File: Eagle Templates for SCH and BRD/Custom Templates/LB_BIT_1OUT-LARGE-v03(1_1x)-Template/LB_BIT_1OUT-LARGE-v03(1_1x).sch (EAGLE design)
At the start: 7 parts, among them P1BSF1 BITSNAP_V03_FEMALE, U6 LV321SOT23-5

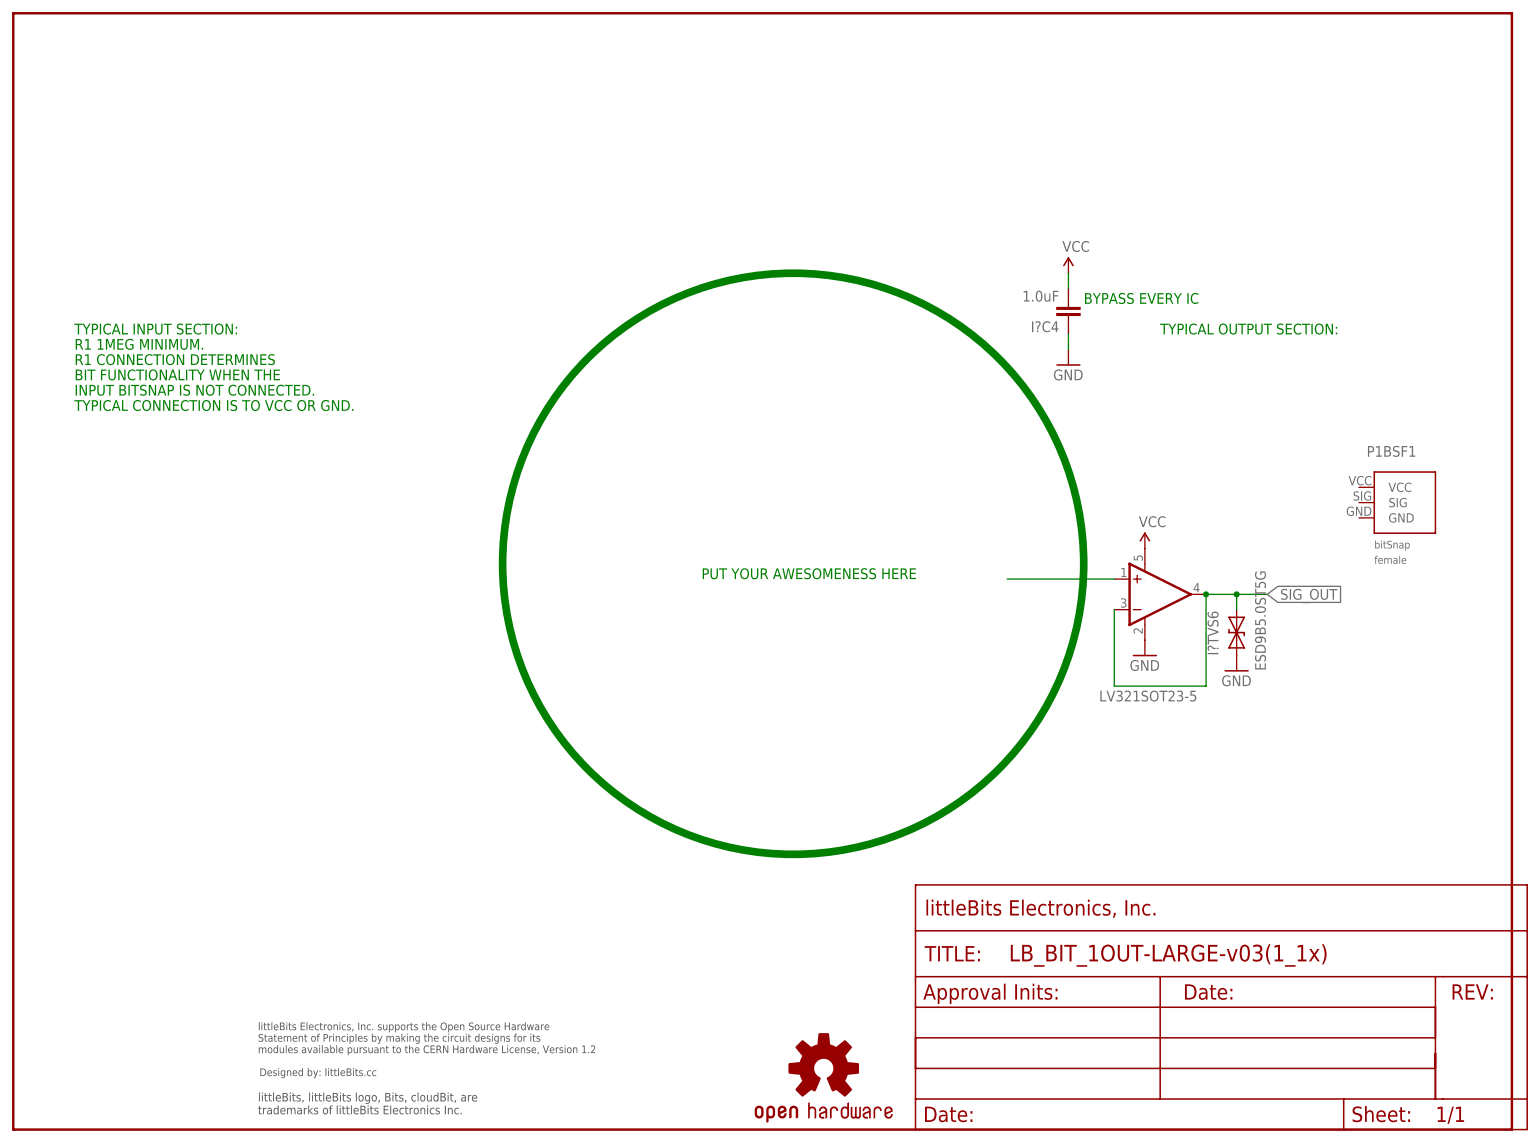
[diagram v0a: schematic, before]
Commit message: Updated templates
- Added ferrite beads
- Moved text and annotations off of Nets layer
- Minor layout changes
- Removed I/O/W prefix from reference designators
- Removed output stage components from output bits
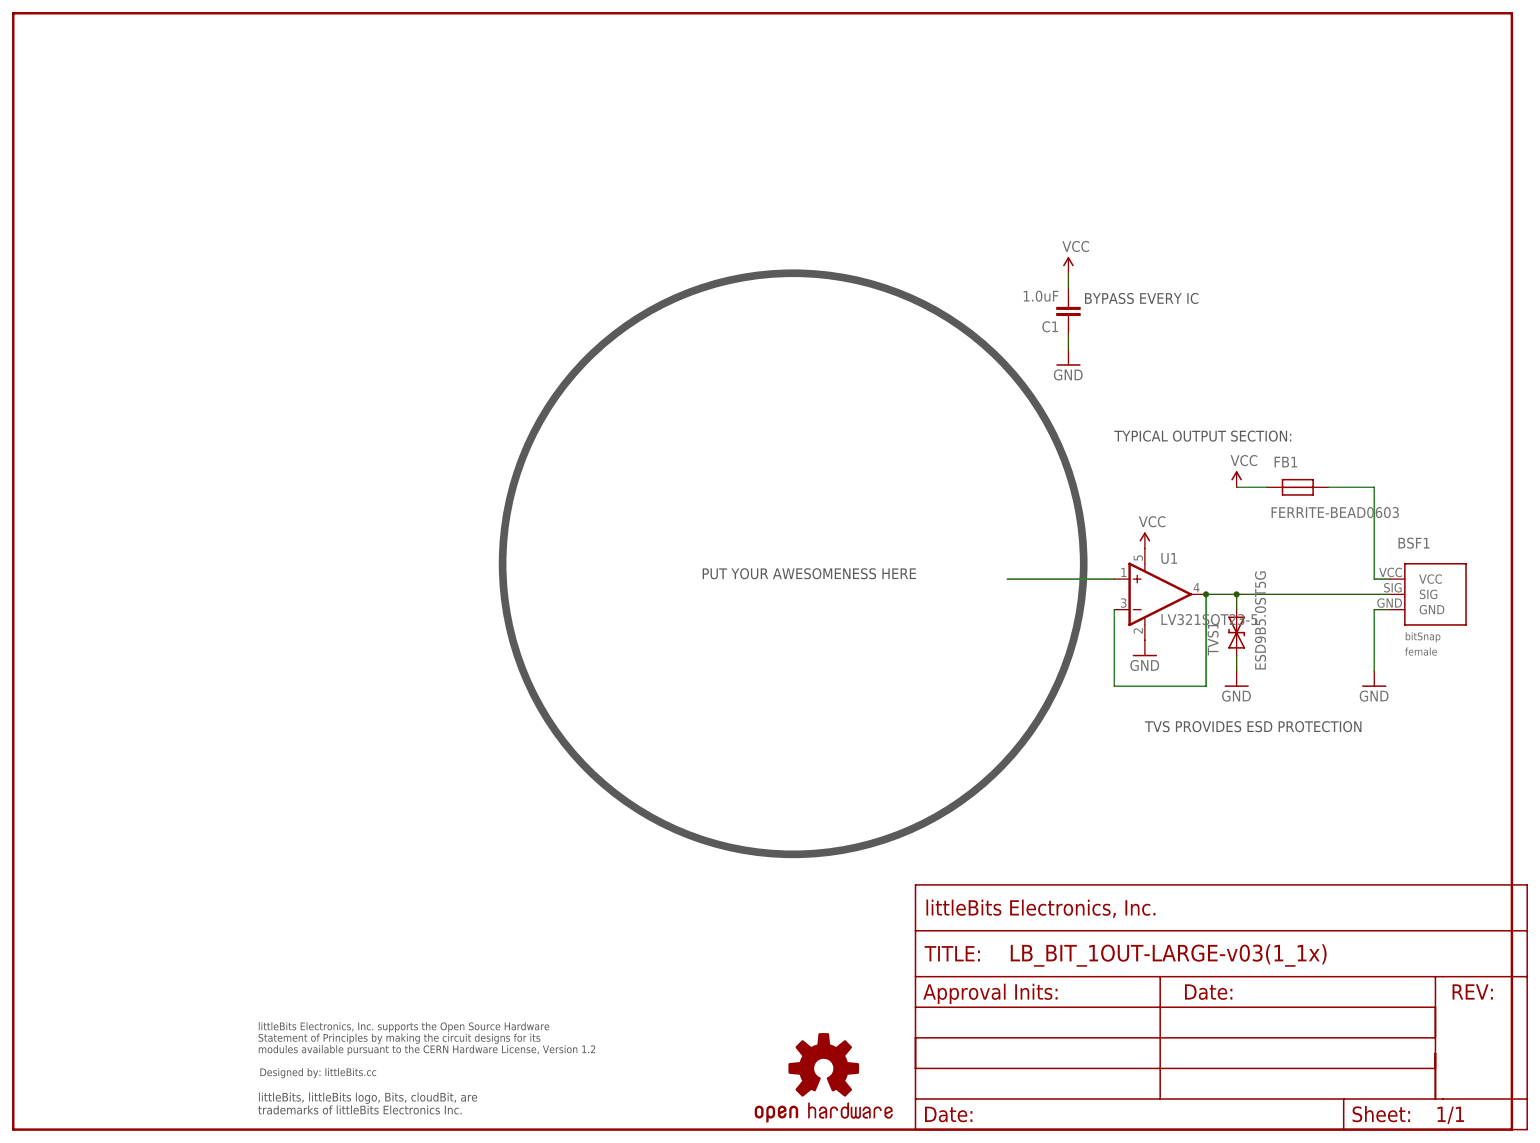
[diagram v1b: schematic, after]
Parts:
- removed P1BSF1: BITSNAP_V03_FEMALE, bitSnap:BITSNAP_V03_FEMALE
- added BSF1: BITSNAP_V03_FEMALE, bitSnap:BITSNAP_V03_FEMALE
- added FB1: FERRITE-BEAD0603, LITTLEBITS:FERRITE-BEAD0603
- FRAME1: value FRAME-LETTER -> FRAME-LETTERWHITEMASK; device LITTLEBITS:FRAME-LETTER -> LITTLEBITS:FRAME-LETTERWHITEMASK
- renumbered I?C4 to C1, I?TVS6 to TVS1, U6 to U1
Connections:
- new net N$2: BSF1.VCC, FB1.P$1
- net GND: now also BSF1.GND
- net SIG_OUT: now also BSF1.SIG
- net VCC: now also FB1.P$2
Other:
- note added: "TVS PROVIDES ESD PROTECTION"
- note removed: "BIT FUNCTIONALITY WHEN THE"
- note removed: "INPUT BITSNAP IS NOT CONNECTED."
- note removed: "R1 1MEG MINIMUM."
- note removed: "R1 CONNECTION DETERMINES"
- note removed: "TYPICAL CONNECTION IS TO VCC OR GND."
- note removed: "TYPICAL INPUT SECTION:"
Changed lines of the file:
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@@
 <?xml version="1.0" encoding="utf-8"?>
 <!DOCTYPE eagle SYSTEM "eagle.dtd">
-<eagle version="6.6.0">
+<eagle version="6.5.0">
 <drawing>
 <settings>
@@
 <layer number="56" name="wert" color="7" fill="1" visible="no" active="no"/>
 <layer number="57" name="tCAD" color="7" fill="1" visible="no" active="no"/>
+<layer number="90" name="Modules" color="5" fill="1" visible="no" active="yes"/>
 <layer number="91" name="Nets" color="2" fill="1" visible="yes" active="yes"/>
 <layer number="92" name="Busses" color="1" fill="1" visible="yes" active="yes"/>
@@
 <layer number="97" name="Info" color="7" fill="1" visible="yes" active="yes"/>
 <layer number="98" name="Guide" color="6" fill="1" visible="yes" active="yes"/>
+<layer number="99" name="SpiceOrder" color="7" fill="1" visible="no" active="no"/>
 <layer number="100" name="Muster" color="7" fill="1" visible="no" active="no"/>
 <layer number="101" name="Patch_Top" color="12" fill="4" visible="yes" active="yes"/>
@@
 <layer number="251" name="SMDround" color="12" fill="11" visible="no" active="no"/>
 <layer number="254" name="cooling" color="7" fill="1" visible="yes" active="yes"/>
+<layer number="255" name="routoute" color="7" fill="1" visible="no" active="yes"/>
 </layers>
 <schematic>
@@
 <parts>
 <part name="U$3" library="SparkFun" deviceset="OSHW-LOGO" device="L"/>
-<part name="P1BSF1" library="bitSnap" deviceset="BITSNAP_V03_FEMALE" device=""/>
-<part name="I?C4" library="LITTLEBITS" deviceset="CAP" device="CAP-0603" value="1.0uF">
+<part name="BSF1" library="bitSnap" deviceset="BITSNAP_V03_FEMALE" device=""/>
+<part name="C1" library="LITTLEBITS" deviceset="CAP" device="CAP-0603" value="1.0uF">
 <attribute name="COMPOSITION" value=""/>
 <attribute name="LB_PN" value=""/>
@@
 <part name="GND17" library="SparkFun" deviceset="GND" device=""/>
 <part name="P+2" library="SparkFun" deviceset="VCC" device=""/>
-<part name="U6" library="LITTLEBITS" deviceset="LV321" device="SOT23-5"/>
+<part name="U1" library="LITTLEBITS" deviceset="LV321" device="SOT23-5"/>
 <part name="GND18" library="SparkFun" deviceset="GND" device=""/>
 <part name="P+3" library="SparkFun" deviceset="VCC" device=""/>
 <part name="GND19" library="SparkFun" deviceset="GND" device=""/>
-<part name="I?TVS6" library="LITTLEBITS" deviceset="DIODE-TVS" device="SOD-923" value="ESD9B5.0ST5G"/>
+<part name="TVS1" library="LITTLEBITS" deviceset="DIODE-TVS" device="SOD-923" value="ESD9B5.0ST5G"/>
 <part name="U$4" library="LITTLEBITS" deviceset="OSHWCREDIT" device=""/>
-<part name="FRAME1" library="LITTLEBITS" deviceset="FRAME-LETTER" device=""/>
+<part name="FRAME1" library="LITTLEBITS" deviceset="FRAME-LETTER" device="WHITEMASK"/>
+<part name="FB1" library="LITTLEBITS" deviceset="FERRITE-BEAD" device="0603"/>
+<part name="GND1" library="SparkFun" deviceset="GND" device=""/>
+<part name="P+1" library="SparkFun" deviceset="VCC" device=""/>
 </parts>
 <sheets>
 <sheet>
 <plain>
-<text x="10.16" y="129.54" size="1.778" layer="91">R1 1MEG MINIMUM.</text>
-<text x="10.16" y="127" size="1.778" layer="91">R1 CONNECTION DETERMINES</text>
-<text x="10.16" y="124.46" size="1.778" layer="91">BIT FUNCTIONALITY WHEN THE</text>
-<text x="10.16" y="121.92" size="1.778" layer="91">INPUT BITSNAP IS NOT CONNECTED.</text>
-<text x="10.16" y="119.38" size="1.778" layer="91">TYPICAL CONNECTION IS TO VCC OR GND.</text>
-<text x="10.16" y="132.08" size="1.778" layer="91">TYPICAL INPUT SECTION:</text>
-<circle x="129.54" y="93.98" radius="48.26" width="1.27" layer="91"/>
-<text x="114.3" y="91.44" size="1.778" layer="91">PUT YOUR AWESOMENESS HERE</text>
-<text x="190.5" y="132.08" size="1.778" layer="91">TYPICAL OUTPUT SECTION:</text>
-<text x="177.8" y="137.16" size="1.778" layer="91">BYPASS EVERY IC</text>
+<circle x="129.54" y="93.98" radius="48.26" width="1.27" layer="97"/>
+<text x="114.3" y="91.44" size="1.778" layer="97">PUT YOUR AWESOMENESS HERE</text>
+<text x="182.88" y="114.3" size="1.778" layer="97">TYPICAL OUTPUT SECTION:</text>
+<text x="177.8" y="137.16" size="1.778" layer="97">BYPASS EVERY IC</text>
+<text x="187.96" y="66.04" size="1.778" layer="97">TVS PROVIDES ESD PROTECTION</text>
 </plain>
 <instances>
 <instance part="U$3" gate="G$1" x="134.62" y="10.16"/>
-<instance part="P1BSF1" gate="G$1" x="226.06" y="99.06"/>
-<instance part="I?C4" gate="G$1" x="175.26" y="137.16" smashed="yes" rot="R180">
+<instance part="BSF1" gate="G$1" x="231.14" y="83.82"/>
+<instance part="C1" gate="G$1" x="175.26" y="137.16" smashed="yes" rot="R180">
 <attribute name="NAME" x="173.736" y="134.239" size="1.778" layer="95" rot="R180"/>
 <attribute name="VALUE" x="173.736" y="139.319" size="1.778" layer="96" rot="R180"/>
@@
 <instance part="GND17" gate="1" x="175.26" y="127"/>
 <instance part="P+2" gate="1" x="175.26" y="142.24"/>
-<instance part="U6" gate="G$1" x="190.5" y="88.9" smashed="yes">
-<attribute name="VALUE" x="180.34" y="71.12" size="1.778" layer="96"/>
-</instance>
+<instance part="U1" gate="G$1" x="190.5" y="88.9"/>
 <instance part="GND18" gate="1" x="187.96" y="78.74"/>
 <instance part="P+3" gate="1" x="187.96" y="96.52"/>
-<instance part="GND19" gate="1" x="203.2" y="76.2"/>
-<instance part="I?TVS6" gate="G$1" x="203.2" y="83.82" smashed="yes">
+<instance part="GND19" gate="1" x="203.2" y="73.66"/>
+<instance part="TVS1" gate="G$1" x="203.2" y="83.82" smashed="yes">
 <attribute name="NAME" x="200.1774" y="78.74" size="1.778" layer="95" rot="R90"/>
 <attribute name="VALUE" x="208.0514" y="76.2" size="1.778" layer="96" rot="R90"/>
@@
 <instance part="FRAME1" gate="G$1" x="0" y="0"/>
 <instance part="FRAME1" gate="G$2" x="149.86" y="0"/>
+<instance part="FB1" gate="G$1" x="213.36" y="106.68"/>
+<instance part="GND1" gate="1" x="226.06" y="73.66"/>
+<instance part="P+1" gate="1" x="203.2" y="106.68"/>
 </instances>
 <busses>
@@
 <segment>
 <pinref part="P+2" gate="1" pin="VCC"/>
-<pinref part="I?C4" gate="G$1" pin="2"/>
+<pinref part="C1" gate="G$1" pin="2"/>
 <wire x1="175.26" y1="142.24" x2="175.26" y2="139.7" width="0.1524" layer="91"/>
 </segment>
 <segment>
-<pinref part="U6" gate="G$1" pin="V+"/>
+<pinref part="U1" gate="G$1" pin="V+"/>
 <pinref part="P+3" gate="1" pin="VCC"/>
 </segment>
+<segment>
+<pinref part="FB1" gate="G$1" pin="P$2"/>
+<wire x1="208.28" y1="106.68" x2="203.2" y2="106.68" width="0.1524" layer="91"/>
+<pinref part="P+1" gate="1" pin="VCC"/>
+</segment>
 </net>
 <net name="GND" class="0">
 <segment>
 <pinref part="GND17" gate="1" pin="GND"/>
-<pinref part="I?C4" gate="G$1" pin="1"/>
+<pinref part="C1" gate="G$1" pin="1"/>
 <wire x1="175.26" y1="132.08" x2="175.26" y2="129.54" width="0.1524" layer="91"/>
 </segment>
 <segment>
-<pinref part="U6" gate="G$1" pin="V-"/>
+<pinref part="U1" gate="G$1" pin="V-"/>
 <pinref part="GND18" gate="1" pin="GND"/>
 </segment>
 <segment>
-<pinref part="I?TVS6" gate="G$1" pin="A"/>
+<pinref part="TVS1" gate="G$1" pin="A"/>
 <pinref part="GND19" gate="1" pin="GND"/>
+<wire x1="203.2" y1="76.2" x2="203.2" y2="78.74" width="0.1524" layer="91"/>
+</segment>
+<segment>
+<pinref part="BSF1" gate="G$1" pin="GND"/>
+<wire x1="228.6" y1="86.36" x2="226.06" y2="86.36" width="0.1524" layer="91"/>
+<pinref part="GND1" gate="1" pin="GND"/>
+<wire x1="226.06" y1="86.36" x2="226.06" y2="76.2" width="0.1524" layer="91"/>
 </segment>
 </net>
 <net name="SIG_OUT" class="0">
 <segment>
-<label x="208.28" y="88.9" size="1.778" layer="95" xref="yes"/>
-</segment>
-<segment>
-<pinref part="U6" gate="G$1" pin="-IN"/>
+<pinref part="U1" gate="G$1" pin="-IN"/>
 <wire x1="182.88" y1="86.36" x2="182.88" y2="73.66" width="0.1524" layer="91"/>
 <wire x1="182.88" y1="73.66" x2="198.12" y2="73.66" width="0.1524" layer="91"/>
-<pinref part="U6" gate="G$1" pin="OUT"/>
+<pinref part="U1" gate="G$1" pin="OUT"/>
 <wire x1="198.12" y1="73.66" x2="198.12" y2="88.9" width="0.1524" layer="91"/>
 <wire x1="198.12" y1="88.9" x2="203.2" y2="88.9" width="0.1524" layer="91"/>
 <junction x="198.12" y="88.9"/>
-<pinref part="I?TVS6" gate="G$1" pin="C"/>
+<pinref part="TVS1" gate="G$1" pin="C"/>
 <wire x1="203.2" y1="86.36" x2="203.2" y2="88.9" width="0.1524" layer="91"/>
-<wire x1="208.28" y1="88.9" x2="203.2" y2="88.9" width="0.1524" layer="91"/>
 <junction x="203.2" y="88.9"/>
+<pinref part="BSF1" gate="G$1" pin="SIG"/>
+<wire x1="203.2" y1="88.9" x2="228.6" y2="88.9" width="0.1524" layer="91"/>
 </segment>
 </net>
 <net name="N$12" class="0">
 <segment>
-<pinref part="U6" gate="G$1" pin="+IN"/>
+<pinref part="U1" gate="G$1" pin="+IN"/>
 <wire x1="182.88" y1="91.44" x2="165.1" y2="91.44" width="0.1524" layer="91"/>
 </segment>
 </net>
+<net name="N$2" class="0">
+<segment>
+<pinref part="FB1" gate="G$1" pin="P$1"/>
+<wire x1="218.44" y1="106.68" x2="226.06" y2="106.68" width="0.1524" layer="91"/>
+<wire x1="226.06" y1="106.68" x2="226.06" y2="91.44" width="0.1524" layer="91"/>
+<pinref part="BSF1" gate="G$1" pin="VCC"/>
+<wire x1="226.06" y1="91.44" x2="228.6" y2="91.44" width="0.1524" layer="91"/>
+</segment>
+</net>
